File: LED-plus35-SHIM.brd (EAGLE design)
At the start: 56 x 65 mm, 138 parts, among them IC1 TXB0101DCKR

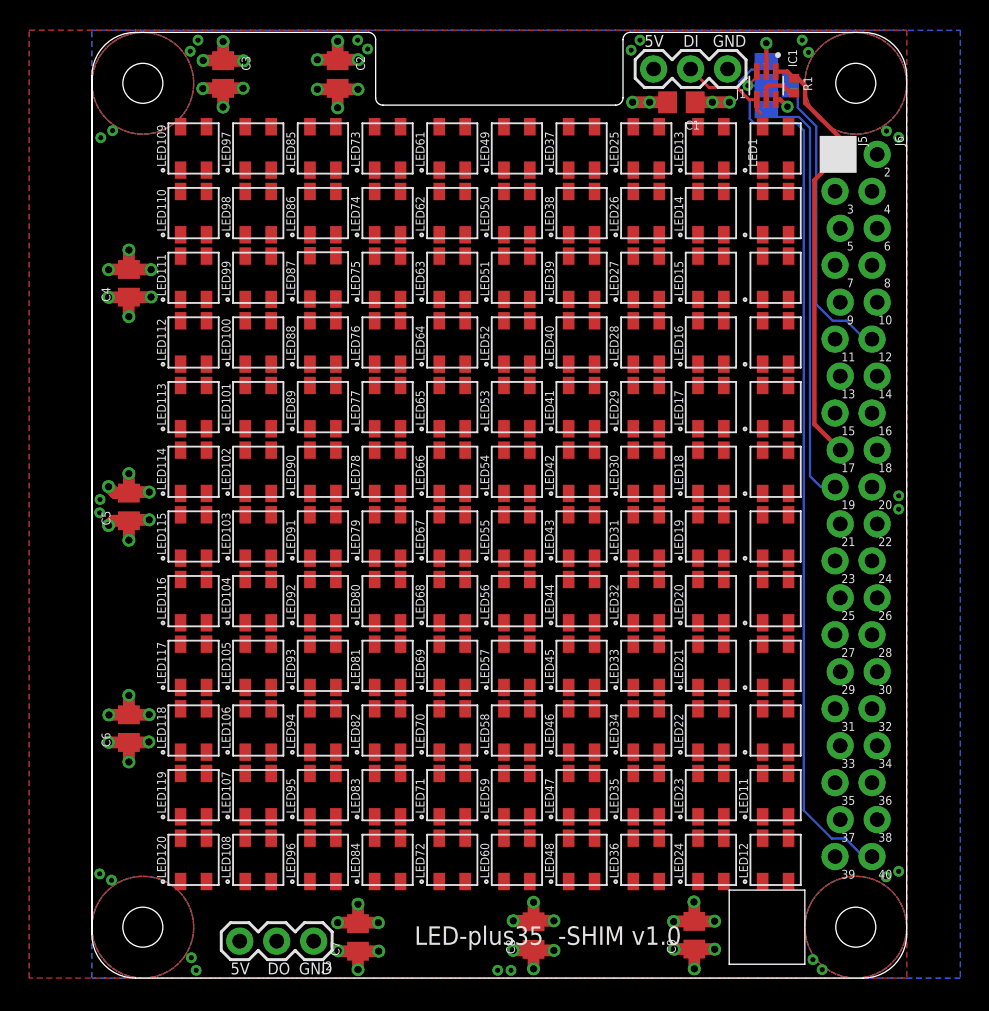
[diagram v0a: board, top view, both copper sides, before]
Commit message: Routed 35 plus board. Generated CAM files. Generated PNG preview. Generated PDF schematics.
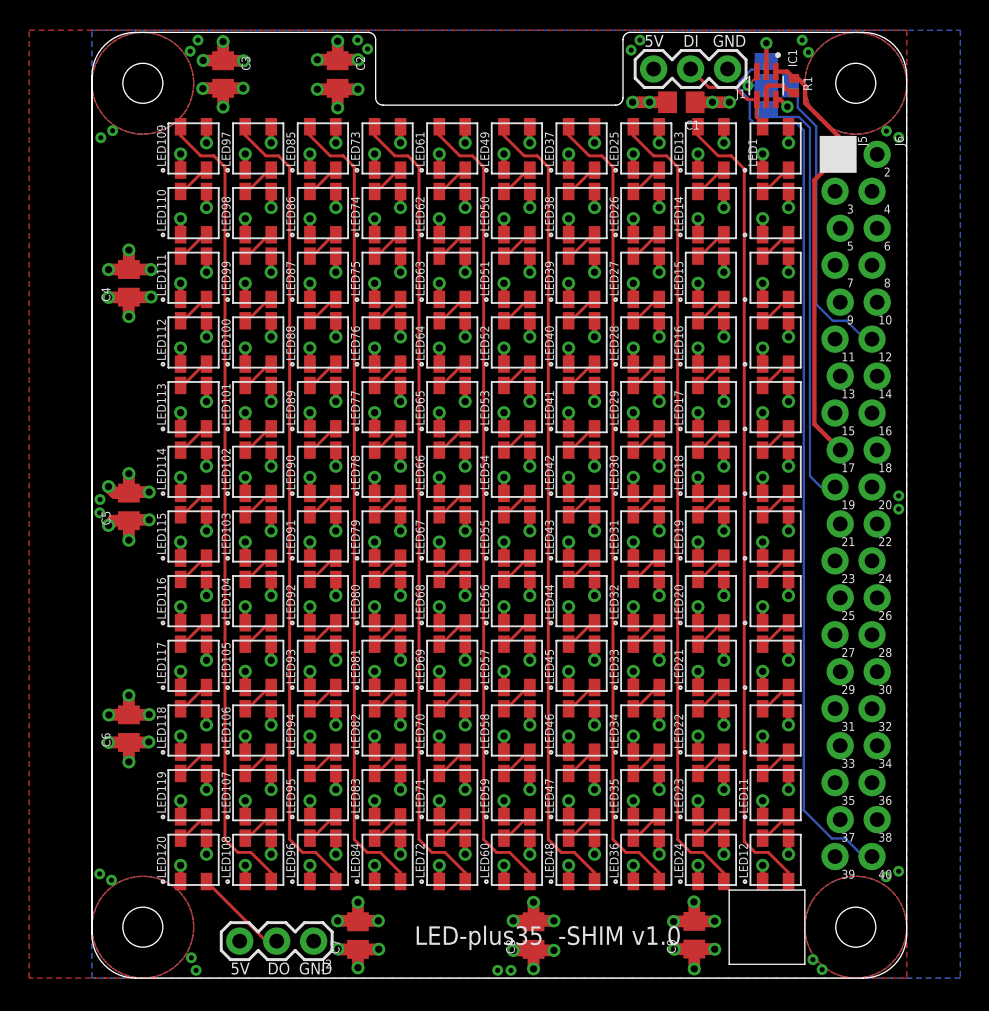
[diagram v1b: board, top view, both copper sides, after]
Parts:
- moved C7 0.13 mm to (18.3, 2.92)
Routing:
- net 5V: track 36.7 -> 169.8 mm, vias 40 -> 160
- net GND: track 37.9 -> 171.0 mm, vias 40 -> 160
- net N$13: track 0.00 -> 55.5 mm
- net N$49: track 0.00 -> 55.5 mm
- net N$85: track 0.00 -> 55.5 mm
- net N$73: track 0.00 -> 55.5 mm
- net N$109: track 0.00 -> 55.5 mm
- net N$97: track 0.00 -> 55.5 mm
- net N$37: track 0.00 -> 55.5 mm
- net N$25: track 0.00 -> 55.5 mm
- net DO_MID: track 0.00 -> 55.5 mm
- net DO_LAST: track 0.00 -> 6.52 mm
- net N$88: track 0.00 -> 2.40 mm
- net N$28: track 0.00 -> 2.39 mm
- net N$99: track 0.00 -> 2.39 mm
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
